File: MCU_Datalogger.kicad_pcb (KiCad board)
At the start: 2 copper layers, 50 x 30.2 mm, 30 parts, among them J1 Conn_01x04_Pin, J2 Conn_01x09_Pin, J3 Conn_01x04_Pin, J4 Conn_02x03_Odd_Even, U1 24LC1025, U2 DS1337S_, U3 24LC1025, U4 ATMEGA328P-AU, Y1 32.768 KHz, Y2 16 MHz

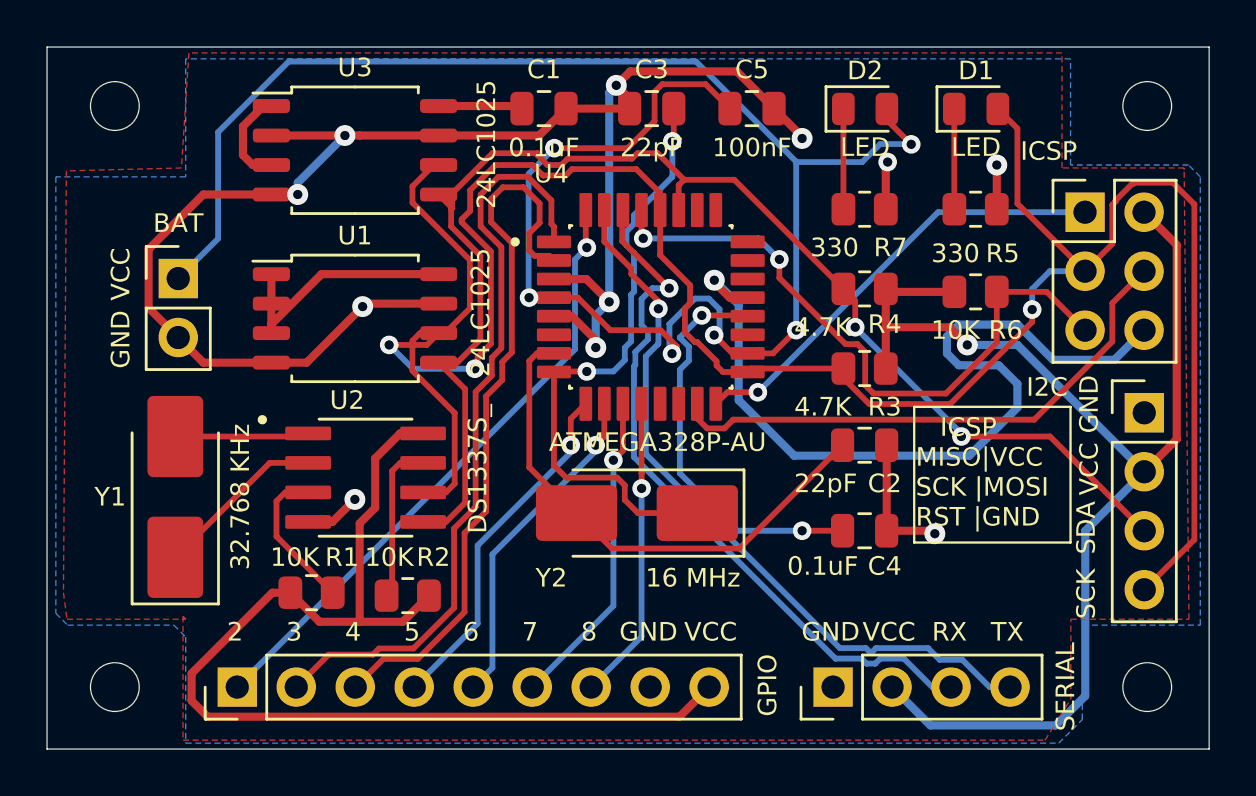
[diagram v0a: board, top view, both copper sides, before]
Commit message: Fixed two defects in the schematic.
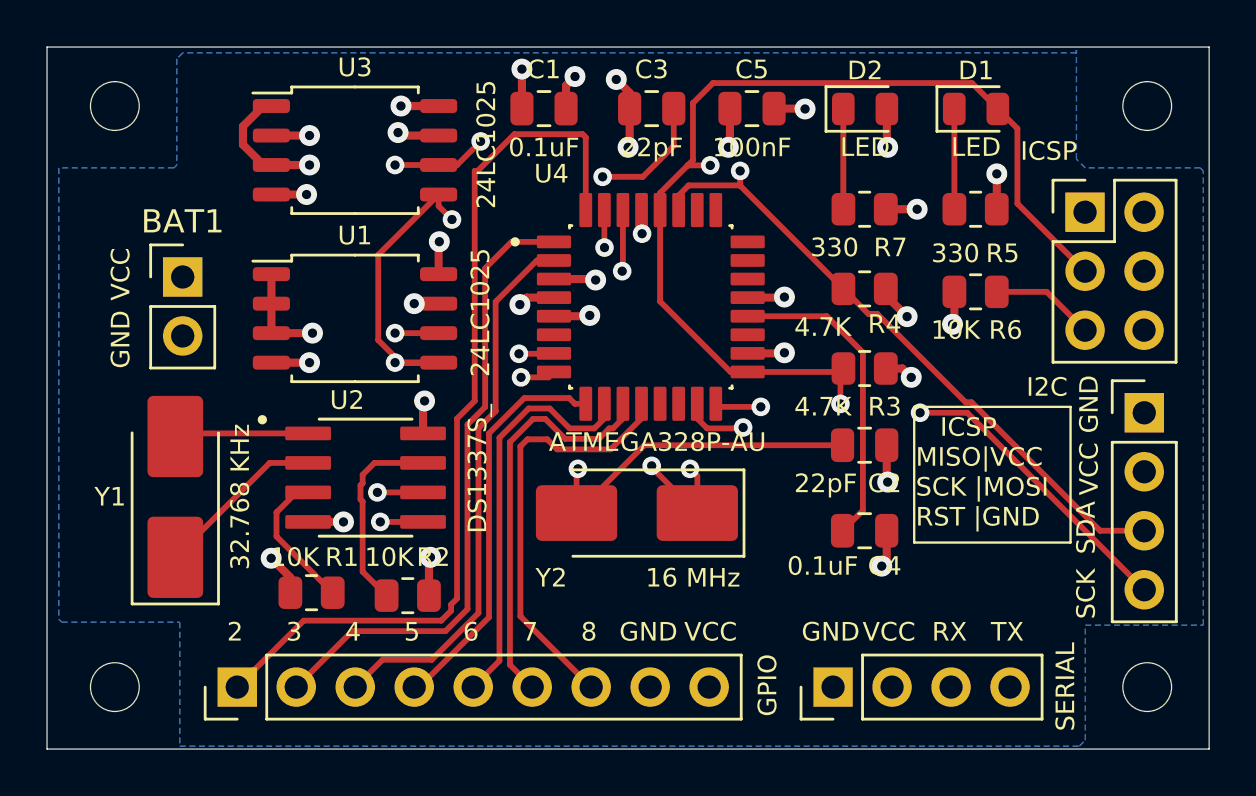
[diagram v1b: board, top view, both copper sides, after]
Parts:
- removed BAT: BS-7, Connector_PinHeader_2.54mm:PinHeader_1x02_P2.54mm_Vertical
- removed REF**: KiCad-Logo2_5mm_SilkScreen, Symbol:KiCad-Logo2_5mm_SilkScreen
- added BAT1: BS-7, Connector_PinHeader_2.54mm:PinHeader_1x02_P2.54mm_Vertical, F.Cu at (141.6, 69.3)
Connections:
- C5 pad 1: Net-(D2-A) -> /VCC
- D2 pad 2: Net-(D2-A) -> /VCC
- U4 pad 18: Net-(D2-A) -> /VCC
- U4 pad 4: Net-(D2-A) -> /VCC
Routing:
- net GND: track 120.3 -> 26.3 mm, vias 12 -> 17
- net /VCC: track 117.9 -> 30.4 mm, vias 1 -> 15
- net Net-(D2-A): track 83.6 -> 0.00 mm, vias 6 -> 0
- net /SCK: track 106.3 -> 92.9 mm, vias 3 -> 7
- net /D2: track 26.8 -> 38.6 mm, vias 1 -> 0
- net Net-(U4-PB7): track 26.6 -> 36.6 mm, vias 2 -> 4
- net /D4: track 31.1 -> 23.6 mm
- net /SDA: track 58.4 -> 64.6 mm, vias 2 -> 4
- net /RESET: track 28.1 -> 34.1 mm, vias 2 -> 1
- net /D3: track 32.8 -> 27.2 mm
- net /D8: track 13.1 -> 18.3 mm, vias 1 -> 0
- net /MISO: track 19.3 -> 23.6 mm
- net Net-(U4-AREF): track 17.5 -> 13.7 mm, vias 2 -> 0
- net /D7: track 13.8 -> 17.6 mm, vias 1 -> 0
- net /D6: track 14.5 -> 17.4 mm, vias 1 -> 0
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- added copper zone on In2.Cu, net /VCC
- removed copper zone on F.Cu, net /VCC
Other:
- copper layers 2 -> 4

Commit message: Fixed all defects.
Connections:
- J1 pad 4: /SCK -> /SCL
- R3 pad 2: /SCK -> /SCL
- U1 pad 6: /SCK -> /SCL
- U2 pad 6: /SCK -> /SCL
- U3 pad 6: /SCK -> /SCL
- U4 pad 28: /SCK -> /SCL
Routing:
- net /SCK: track 92.9 -> 28.5 mm, vias 7 -> 2
- net /SCL: track 0.00 -> 63.5 mm, vias 0 -> 7
- net /D2: track 38.6 -> 31.7 mm
- net GND: track 26.3 -> 25.4 mm
